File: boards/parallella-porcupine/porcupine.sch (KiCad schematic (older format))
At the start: 0 parts

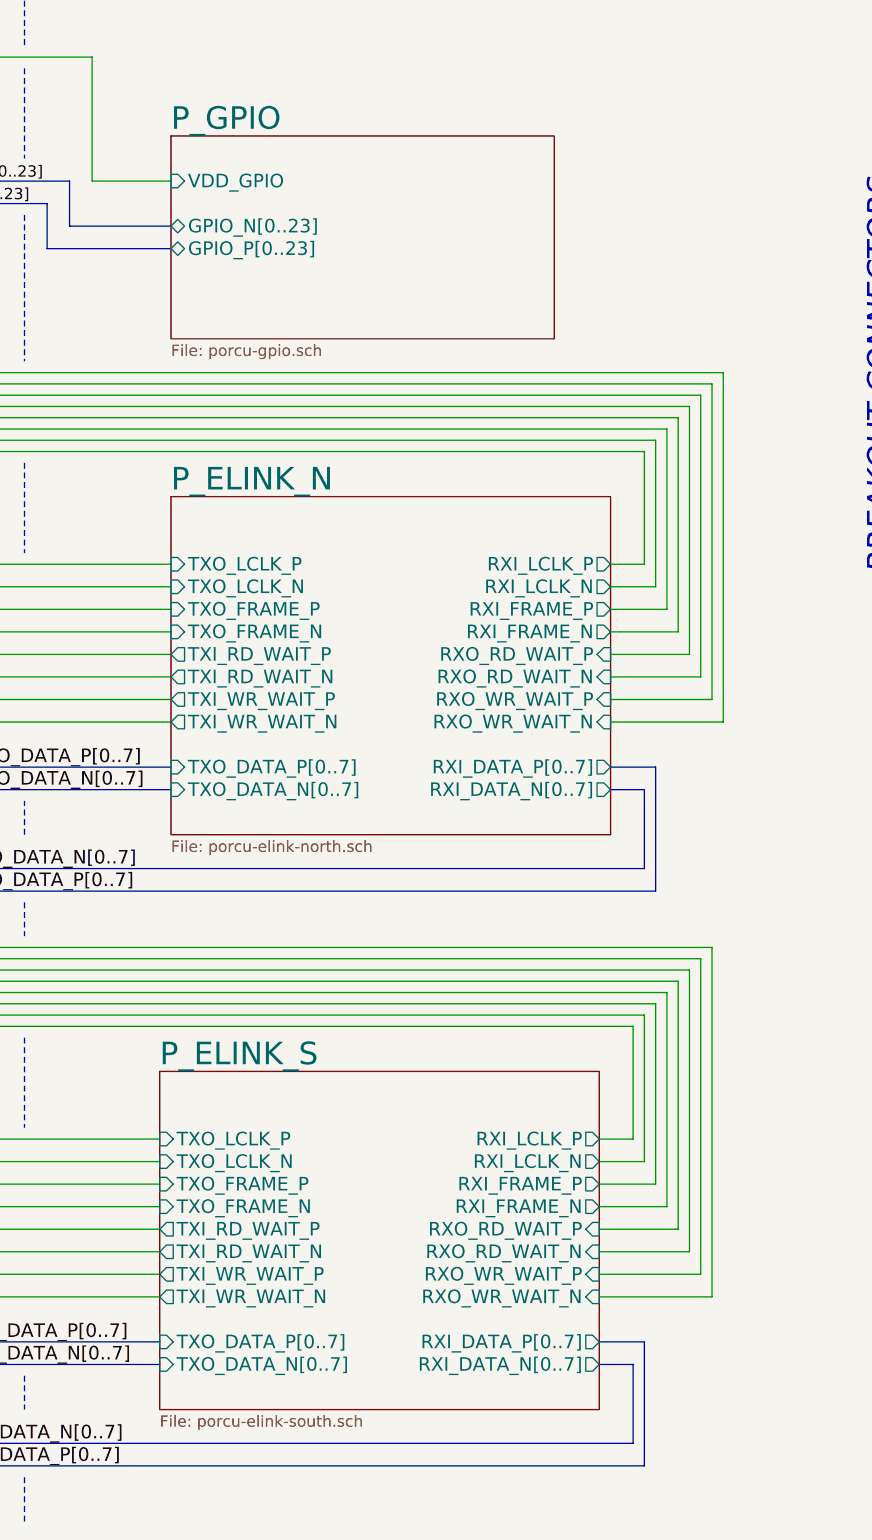
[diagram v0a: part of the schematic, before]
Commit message: Schematic is stable, PCB mostly routed.
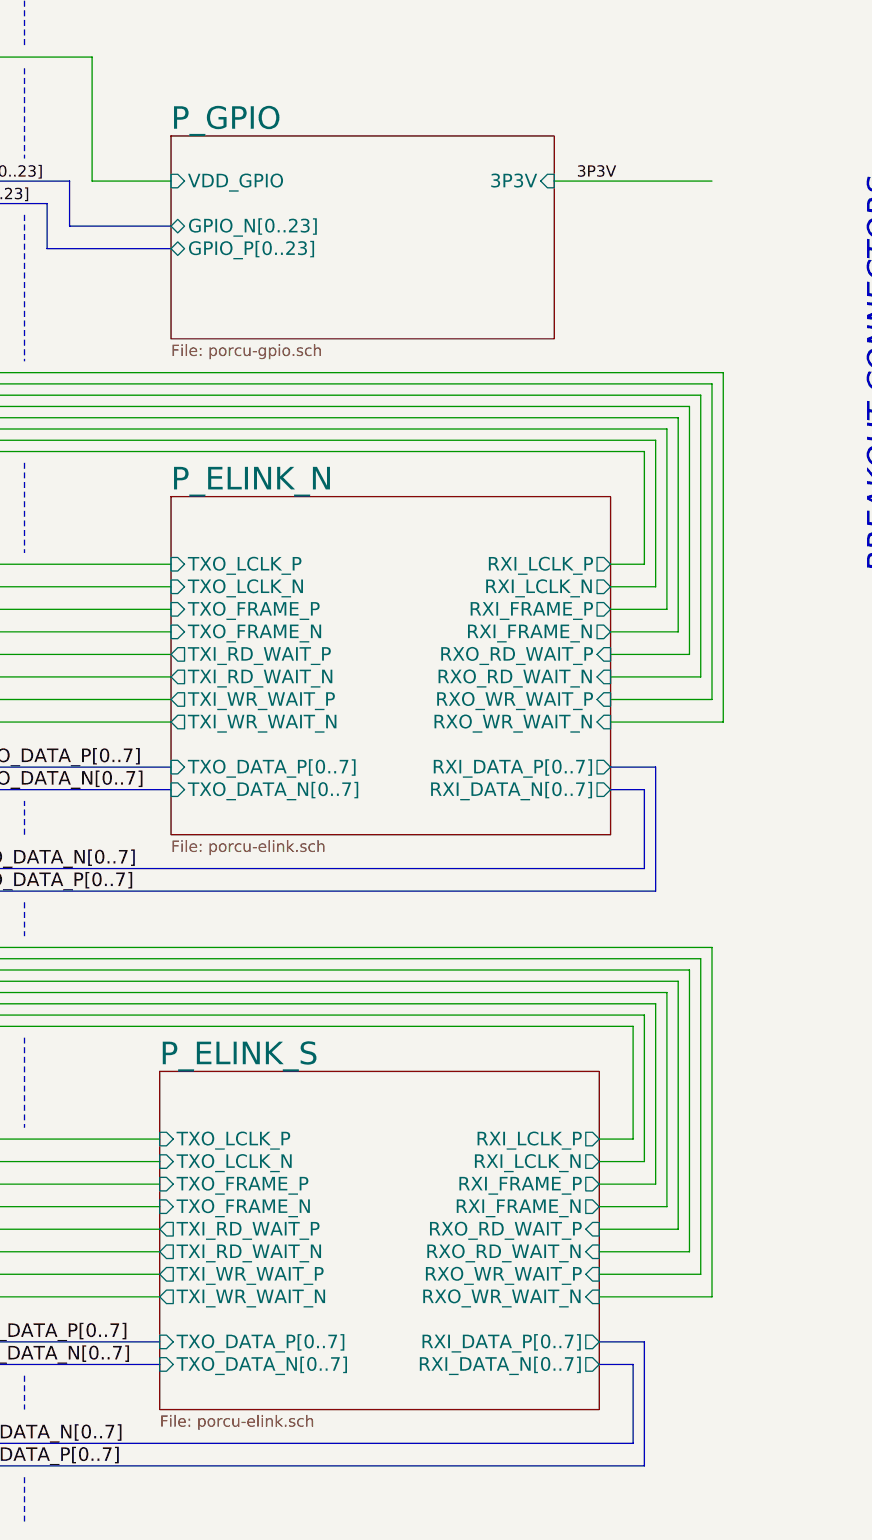
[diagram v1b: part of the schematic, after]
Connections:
- wire segments 144 -> 145
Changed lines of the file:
@@
 F3 "GPIO_N[0..23]" B L 7250 4600 60
 F4 "GPIO_P[0..23]" B L 7250 4700 60
+F5 "3P3V" I R 8950 4400 60
 $EndSheet
 $Sheet
@@
 U 538C99D9
 F0 "P_ELINK_N" 100
-F1 "porcu-elink-north.sch" 50
+F1 "porcu-elink.sch" 50
 F2 "RXI_FRAME_N" O R 9200 6400 60
 F3 "RXI_FRAME_P" O R 9200 6300 60
@@
 U 538F26CD
 F0 "P_ELINK_S" 100
-F1 "porcu-elink-south.sch" 50
+F1 "porcu-elink.sch" 50
 F2 "RXI_FRAME_N" O R 9150 8950 60
 F3 "RXI_FRAME_P" O R 9150 8850 60
@@
 Wire Notes Line
 	6600 7600 6600 7750
+Wire Wire Line
+	9650 4400 8950 4400
+Text Label 9050 4400 0    50   ~ 0
+3P3V
 $EndSCHEMATC

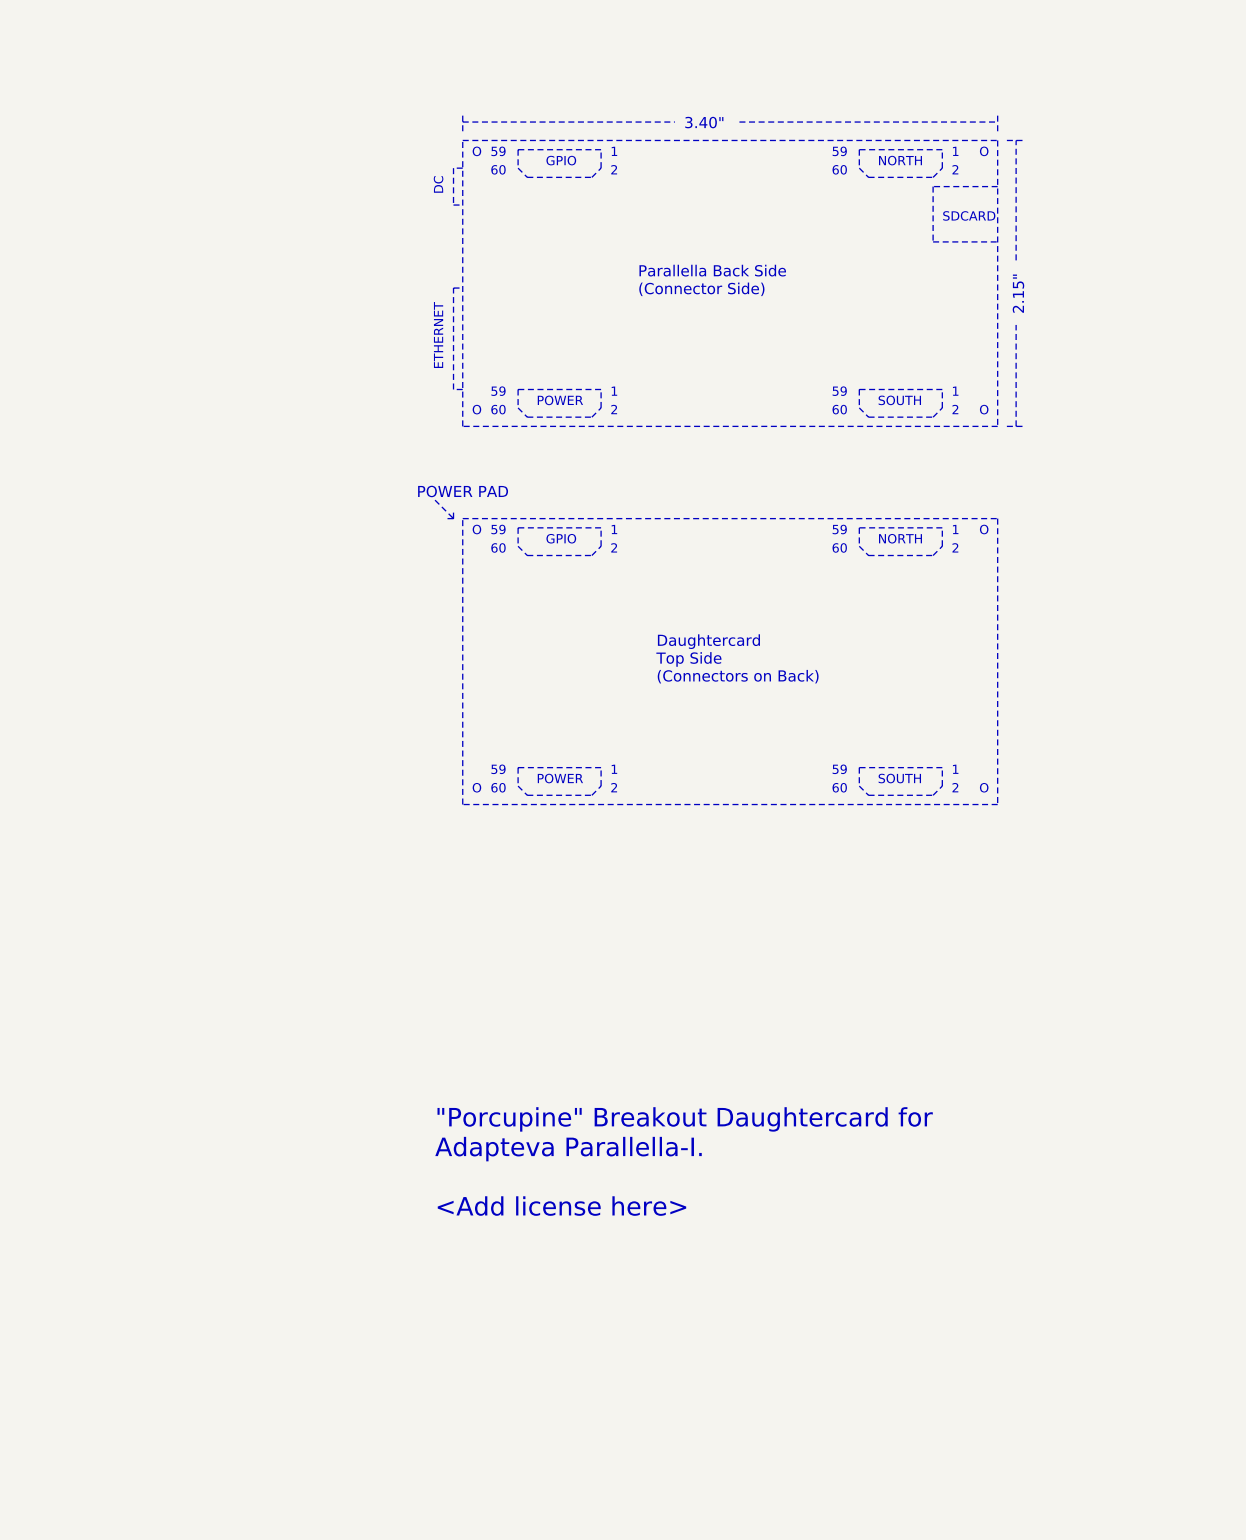
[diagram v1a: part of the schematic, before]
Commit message: Completed design w/3-row XID/YID and various 4-pin IO connectors. Fixed page ordering, changed "Mfr" field to "Manufacturer" Will now re-do to combine all misc. functions onto a single 2xN connector.
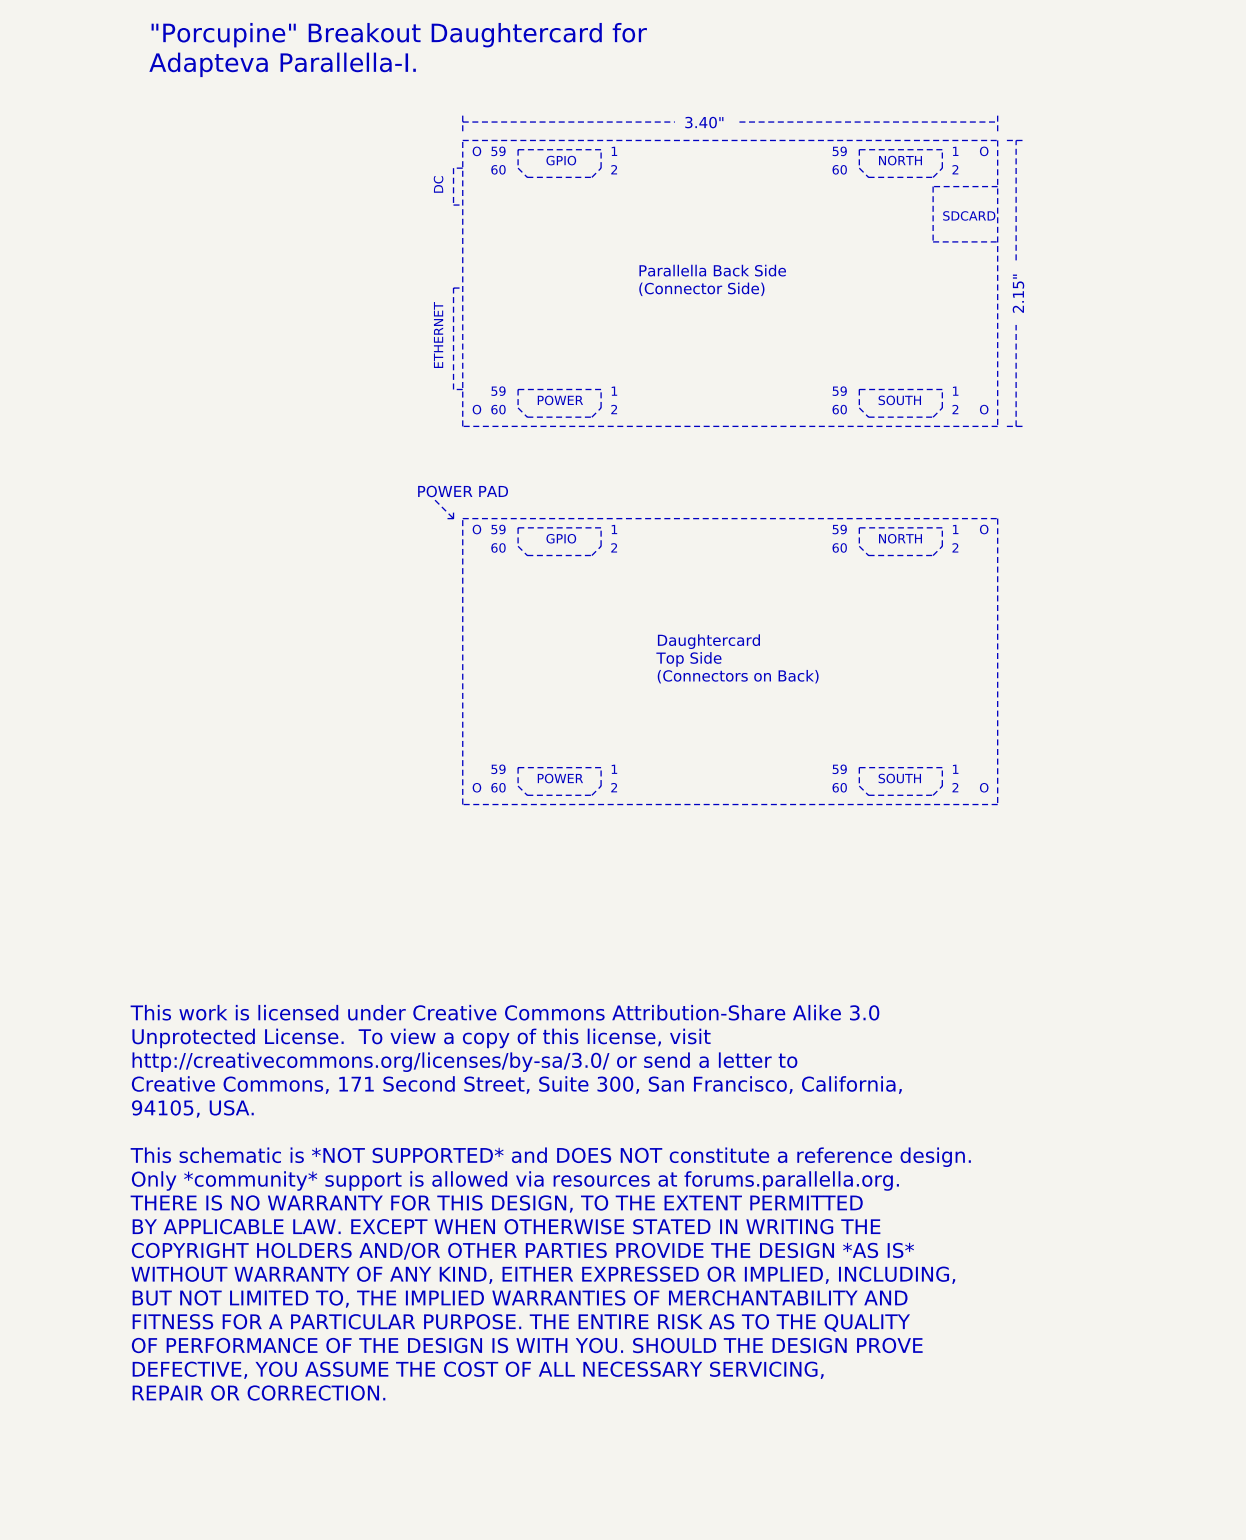
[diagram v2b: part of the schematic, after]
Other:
- note added: ""Porcupine" Breakout Daughtercard for\nAdapteva Parallella-I."
- note added: "This work is licensed under Creative Commons Attribution-Share Alike 3.0\nUnprotected License. To view a copy of this license, visit \nhttp://creativecommons.org/licenses/by-sa/3.0/ or send a letter to \nCreative Commons, 171 Second Street, Suite 300, San Francisco, California,\n94105, USA.\n\nThis schematic is *NOT SUPPORTED* and DOES NOT constitute a reference design.\nOnly *community* support 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"
- note removed: ""Porcupine" Breakout Daughtercard for\nAdapteva Parallella-I.\n\n<Add license here>\n"
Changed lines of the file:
@@
 Text Notes 16000 2300 1    60   ~ 0
 2.15"
-Text Notes 12800 7200 0    100  ~ 0
-"Porcupine" Breakout Daughtercard for\nAdapteva Parallella-I.\n\n<Add license here>\n
+Text Notes 11250 1000 0    100  ~ 0
+"Porcupine" Breakout Daughtercard for\nAdapteva Parallella-I.
+$Sheet
+S 4150 1000 1900 2200
+U 538682E8
+F0 "POWER" 100
+F1 "paracard-power.sch" 60
+F2 "I2C_SDA" B R 6050 1150 60
+F3 "I2C_SCL" B R 6050 1250 60
+F4 "PROG_IO" B R 6050 1450 60
+F5 "UART_RX" I R 6050 1850 60
+F6 "UART_TX" O R 6050 1950 60
+F7 "USER_LED" O R 6050 1550 60
+F8 "RESET_N" B R 6050 2150 60
+F9 "VADC_P" I R 6050 2350 60
+F10 "JTAG_TDI" I L 4150 2750 60
+F11 "JTAG_TDO" O L 4150 2850 60
+F12 "DSP_FLAG" O R 6050 1650 60
+F13 "TURBO_MODE" O R 6050 2850 60
+F14 "SPDIF" O R 6050 2650 60
+F15 "JTAG_BOOT_EN" I L 4150 2650 60
+F16 "VADC_N" I R 6050 2450 60
+F17 "JTAG_TMS" I L 4150 2950 60
+F18 "JTAG_TCK" I L 4150 3050 60
+F19 "1P0V" I L 4150 1750 60
+F20 "VDD_DSP" I L 4150 1850 60
+F21 "1P35V" I L 4150 1950 60
+F22 "1P8V" I L 4150 2050 60
+F23 "VDD_ADJ" I L 4150 2150 60
+F24 "VDD_GPIO" I L 4150 2250 60
+F25 "2P5V" I L 4150 2350 60
+F26 "3P3V" I L 4150 2450 60
+F27 "SYS_5P0V" O L 4150 1150 60
+F28 "REG_EN[1..4]" I L 4150 1650 60
+F29 "DSP_YID[0..3]" I L 4150 1350 60
+F30 "DSP_XID[0..3]" I L 4150 1450 60
+$EndSheet
 $Sheet
 S 4150 4200 1900 900
@@
 $EndSheet
 $Sheet
-S 4150 1000 1900 2200
-U 538682E8
-F0 "POWER" 100
-F1 "paracard-power.sch" 60
-F2 "I2C_SDA" B R 6050 1150 60
-F3 "I2C_SCL" B R 6050 1250 60
-F4 "PROG_IO" B R 6050 1450 60
-F5 "UART_RX" I R 6050 1850 60
-F6 "UART_TX" O R 6050 1950 60
-F7 "USER_LED" O R 6050 1550 60
-F8 "RESET_N" B R 6050 2150 60
-F9 "VADC_P" I R 6050 2350 60
-F10 "JTAG_TDI" I L 4150 2750 60
-F11 "JTAG_TDO" O L 4150 2850 60
-F12 "DSP_FLAG" O R 6050 1650 60
-F13 "TURBO_MODE" O R 6050 2850 60
-F14 "SPDIF" O R 6050 2650 60
-F15 "JTAG_BOOT_EN" I L 4150 2650 60
-F16 "VADC_N" I R 6050 2450 60
-F17 "JTAG_TMS" I L 4150 2950 60
-F18 "JTAG_TCK" I L 4150 3050 60
-F19 "1P0V" I L 4150 1750 60
-F20 "VDD_DSP" I L 4150 1850 60
-F21 "1P35V" I L 4150 1950 60
-F22 "1P8V" I L 4150 2050 60
-F23 "VDD_ADJ" I L 4150 2150 60
-F24 "VDD_GPIO" I L 4150 2250 60
-F25 "2P5V" I L 4150 2350 60
-F26 "3P3V" I L 4150 2450 60
-F27 "SYS_5P0V" O L 4150 1150 60
-F28 "REG_EN[1..4]" I L 4150 1650 60
-F29 "DSP_YID[0..3]" I L 4150 1350 60
-F30 "DSP_XID[0..3]" I L 4150 1450 60
+S 4100 8350 1900 1500
+U 538F26B7
+F0 "SOUTH" 100
+F1 "paracard-elink.sch" 60
+F2 "VDDIO" O L 4100 8450 60
+F3 "RXI_FRAME_N" I L 4100 8950 60
+F4 "RXI_FRAME_P" I L 4100 8850 60
+F5 "RXO_WR_WAIT_N" O L 4100 9350 60
+F6 "RXO_WR_WAIT_P" O L 4100 9250 60
+F7 "TXI_WR_WAIT_N" I R 6000 9350 60
+F8 "TXI_WR_WAIT_P" I R 6000 9250 60
+F9 "TXI_RD_WAIT_N" I R 6000 9150 60
+F10 "TXI_RD_WAIT_P" I R 6000 9050 60
+F11 "RXI_LCLK_N" I L 4100 8750 60
+F12 "RXI_LCLK_P" I L 4100 8650 60
+F13 "RXO_RD_WAIT_N" O L 4100 9150 60
+F14 "RXO_RD_WAIT_P" O L 4100 9050 60
+F15 "TXO_FRAME_N" O R 6000 8950 60
+F16 "TXO_FRAME_P" O R 6000 8850 60
+F17 "TXO_LCLK_N" O R 6000 8750 60
+F18 "TXO_LCLK_P" O R 6000 8650 60
+F19 "RXI_DATA_N[0..7]" I L 4100 9650 60
+F20 "RXI_DATA_P[0..7]" I L 4100 9550 60
+F21 "TXO_DATA_P[0..7]" O R 6000 9550 60
+F22 "TXO_DATA_N[0..7]" O R 6000 9650 60
 $EndSheet
 $Sheet
@@
 Text Notes 12700 3300 0    60   ~ 0
 POWER PAD
-$Sheet
-S 7250 4200 1700 900
-U 538C90E5
-F0 "P_GPIO" 100
-F1 "porcu-gpio.sch" 50
-F2 "VDD_GPIO" I L 7250 4400 60
-F3 "GPIO_N[0..23]" B L 7250 4600 60
-F4 "GPIO_P[0..23]" B L 7250 4700 60
-F5 "3P3V" I R 8950 4400 60
-$EndSheet
 $Sheet
 S 7250 1000 1700 2200
@@
 $EndSheet
 $Sheet
+S 7250 4200 1700 900
+U 538C90E5
+F0 "P_GPIO" 100
+F1 "porcu-gpio.sch" 50
+F2 "VDD_GPIO" I L 7250 4400 60
+F3 "GPIO_N[0..23]" B L 7250 4600 60
+F4 "GPIO_P[0..23]" B L 7250 4700 60
+F5 "3P3V" I R 8950 4400 60
+$EndSheet
+$Sheet
 S 7250 5800 1950 1500
 U 538C99D9
@@
 Text Label 6200 7550 0    60   ~ 0
 RXI_NO_DATA_P[0..7]
-$Sheet
-S 4100 8350 1900 1500
-U 538F26B7
-F0 "SOUTH" 100
-F1 "paracard-elink.sch" 60
-F2 "VDDIO" O L 4100 8450 60
-F3 "RXI_FRAME_N" I L 4100 8950 60
-F4 "RXI_FRAME_P" I L 4100 8850 60
-F5 "RXO_WR_WAIT_N" O L 4100 9350 60
-F6 "RXO_WR_WAIT_P" O L 4100 9250 60
-F7 "TXI_WR_WAIT_N" I R 6000 9350 60
-F8 "TXI_WR_WAIT_P" I R 6000 9250 60
-F9 "TXI_RD_WAIT_N" I R 6000 9150 60
-F10 "TXI_RD_WAIT_P" I R 6000 9050 60
-F11 "RXI_LCLK_N" I L 4100 8750 60
-F12 "RXI_LCLK_P" I L 4100 8650 60
-F13 "RXO_RD_WAIT_N" O L 4100 9150 60
-F14 "RXO_RD_WAIT_P" O L 4100 9050 60
-F15 "TXO_FRAME_N" O R 6000 8950 60
-F16 "TXO_FRAME_P" O R 6000 8850 60
-F17 "TXO_LCLK_N" O R 6000 8750 60
-F18 "TXO_LCLK_P" O R 6000 8650 60
-F19 "RXI_DATA_N[0..7]" I L 4100 9650 60
-F20 "RXI_DATA_P[0..7]" I L 4100 9550 60
-F21 "TXO_DATA_P[0..7]" O R 6000 9550 60
-F22 "TXO_DATA_N[0..7]" O R 6000 9650 60
-$EndSheet
 $Sheet
 S 7200 8350 1950 1500
@@
 Text Label 9050 4400 0    50   ~ 0
 3P3V
+Text Notes 11150 8200 0    80   ~ 0
+This work is licensed under Creative Commons Attribution-Share Alike 3.0\nUnprotected License.  To view a copy of this license, visit \nhttp://creativecommons.org/licenses/by-sa/3.0/ or send a letter to \nCreative Commons, 171 Second Street, Suite 300, San Francisco, California,\n94105, USA.\n\nThis schematic is *NOT SUPPORTED* and DOES NOT constitute a reference design.\nOnly *community* support is allowed via resources at forums.parallella.org.\nTHERE IS NO WARRANTY FOR THIS DESIGN, TO THE EXTENT PERMITTED\nBY APPLICABLE LAW. EXCEPT WHEN OTHERWISE STATED IN WRITING THE\nCOPYRIGHT HOLDERS AND/OR OTHER PARTIES PROVIDE THE DESIGN *AS IS*\nWITHOUT WARRANTY OF ANY KIND, EITHER EXPRESSED OR IMPLIED, INCLUDING,\nBUT NOT LIMITED TO, THE IMPLIED WARRANTIES OF MERCHANTABILITY AND\nFITNESS FOR A PARTICULAR PURPOSE. THE ENTIRE RISK AS TO THE QUALITY\nOF PERFORMANCE OF THE DESIGN IS WITH YOU. SHOULD THE DESIGN PROVE\nDEFECTIVE, YOU ASSUME THE COST OF ALL NECESSARY SERVICING,\nREPAIR OR CORRECTION.
 $EndSCHEMATC

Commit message: Ready for full review.
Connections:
- wire segments 145 -> 146
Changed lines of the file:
@@
 Sheet 1 10
 Title "Parallella Breakout Daughtercard"
-Date "09 May 2014"
+Date "19 Jun 2014"
 Rev "*"
 Comp "Adapteva, Inc., 1666 Massachusetts Ave., Lexington, MA, 02420"
@@
 F29 "DSP_YID[0..3]" I L 4150 1350 60
 F30 "DSP_XID[0..3]" I L 4150 1450 60
+F31 "SPARE" B R 6050 2950 60
 $EndSheet
 $Sheet
@@
 F30 "JTAG_TCK" O R 8950 3050 60
 F31 "MH_SYSPWR" I L 7250 3050 60
+F32 "SPARE" B L 7250 2950 60
 $EndSheet
 $Sheet
@@
 	6600 800  6600 1100
 Wire Notes Line
-	6600 2900 6600 3500
-Wire Notes Line
 	6600 3900 6600 4300
 Wire Notes Line
@@
 Text Notes 11150 8200 0    80   ~ 0
 This work is licensed under Creative Commons Attribution-Share Alike 3.0\nUnprotected License.  To view a copy of this license, visit \nhttp://creativecommons.org/licenses/by-sa/3.0/ or send a letter to \nCreative Commons, 171 Second Street, Suite 300, San Francisco, California,\n94105, USA.\n\nThis schematic is *NOT SUPPORTED* and DOES NOT constitute a reference design.\nOnly *community* support is allowed via resources at forums.parallella.org.\nTHERE IS NO WARRANTY FOR THIS DESIGN, TO THE EXTENT PERMITTED\nBY APPLICABLE LAW. EXCEPT WHEN OTHERWISE STATED IN WRITING THE\nCOPYRIGHT HOLDERS AND/OR OTHER PARTIES PROVIDE THE DESIGN *AS IS*\nWITHOUT WARRANTY OF ANY KIND, EITHER EXPRESSED OR IMPLIED, INCLUDING,\nBUT NOT LIMITED TO, THE IMPLIED WARRANTIES OF MERCHANTABILITY AND\nFITNESS FOR A PARTICULAR PURPOSE. THE ENTIRE RISK AS TO THE QUALITY\nOF PERFORMANCE OF THE DESIGN IS WITH YOU. SHOULD THE DESIGN PROVE\nDEFECTIVE, YOU ASSUME THE COST OF ALL NECESSARY SERVICING,\nREPAIR OR CORRECTION.
+Wire Wire Line
+	6050 2950 7250 2950
+Wire Notes Line
+	6600 3500 6600 3000
 $EndSCHEMATC

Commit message: Porcupine Version 2.
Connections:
- net labels added: VGPIO
- wire segments 146 -> 148
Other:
- note added: ""Porcupine" Breakout Daughtercard for\nAdapteva Parallella-I.\n Ver. 2: Added Camera Connector"
- note removed: ""Porcupine" Breakout Daughtercard for\nAdapteva Parallella-I."
